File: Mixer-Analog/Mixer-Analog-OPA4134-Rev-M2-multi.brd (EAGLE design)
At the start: 123 x 51 mm, 119 parts, among them IC1 BQ297X, IC2 MCP73831, IC3 QS6K1, IC4 OPA4134D, IC5 SC4503, IC6 TPS7A49, J10 PHONES-OUT, J11 12V, J7 Battery, J9 LINE-OUT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

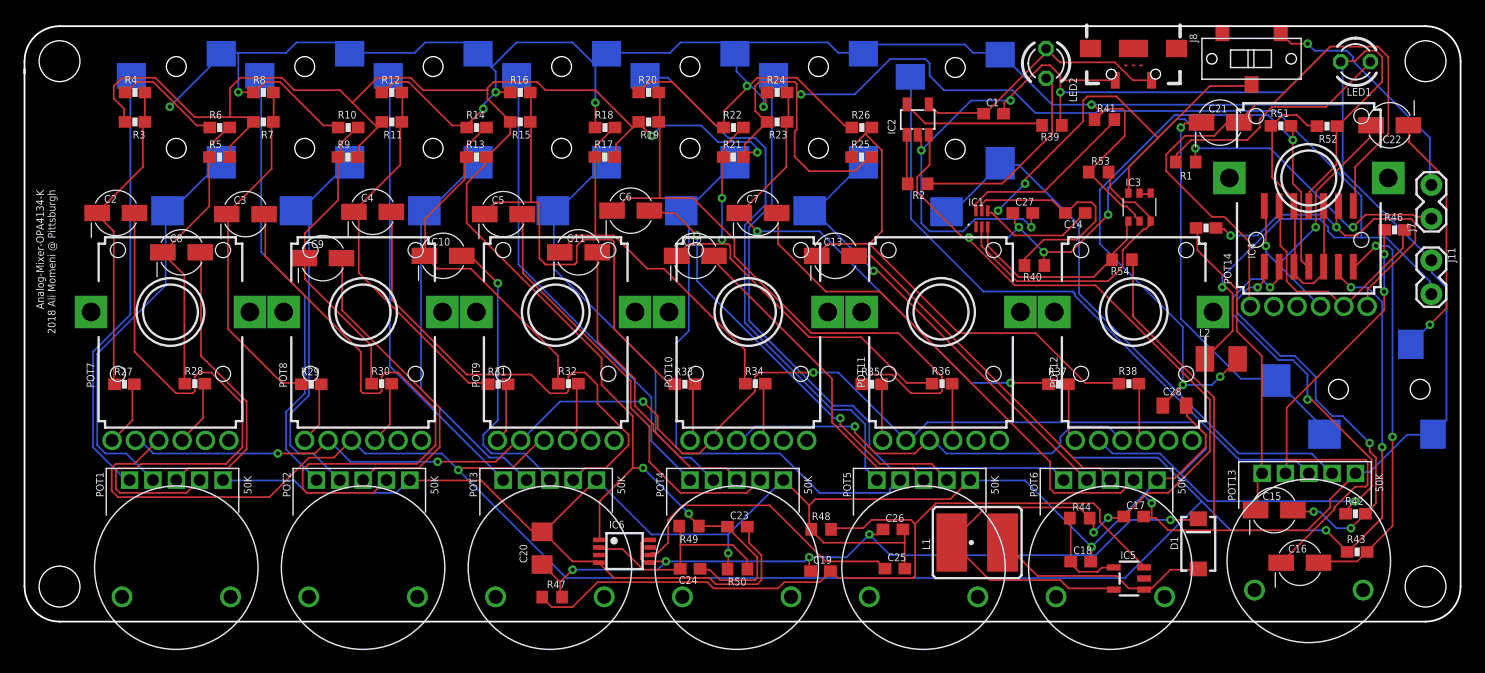
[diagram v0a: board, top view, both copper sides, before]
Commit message: Multiple updates
Rev-M updated for change of capacitors from tantalum to electrolytic.
Rev-M2 created based on the new schematic provided.
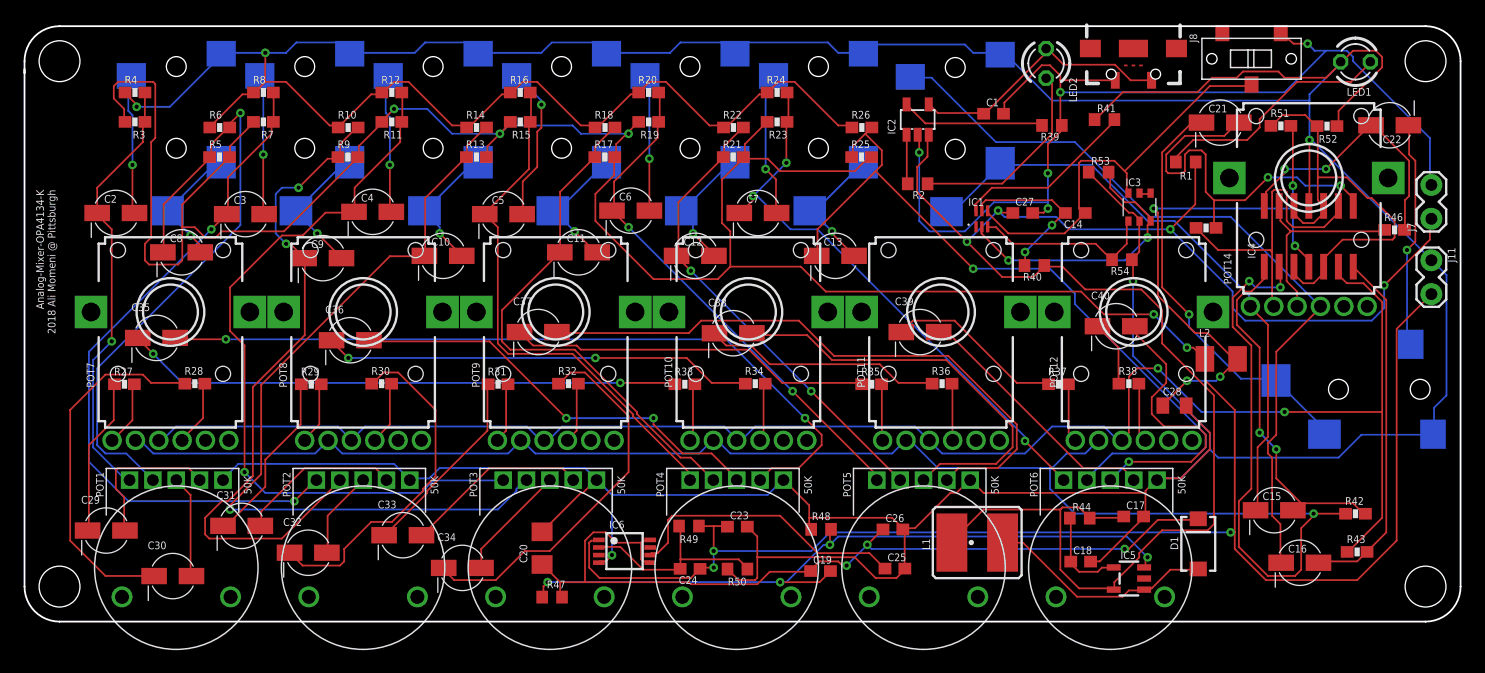
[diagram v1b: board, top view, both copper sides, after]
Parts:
- removed POT13: 50K, CMU-ArtFab:POT-DUAL-ALPS-RK10J12E0A0A
- added C29, C30, C31, C32, C33, C34, C35, C36, C37, C38, C39, C40: 10uF, CMU-ArtFab:PANASONIC_B
- R45, R46: value 47K -> 100K
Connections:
- removed net N$16: J9.2, J9.4, POT13.P$2
- removed net N$18: J9.3, POT13.P$3
- removed net N$76: J5.3, POT5.P$5
- removed net N$80: J5.2, J5.4, POT5.P$4
- removed net N$92: J6.3, POT6.P$5
- removed net N$96: J6.2, J6.4, POT6.P$4
- new net N$20: C30.-, R28.1
- new net N$35: C29.-, R27.1
- new net N$36: C32.-, R30.1
- new net N$37: C32.+, POT2.P$3
- new net N$38: C33.+, POT3.P$2
- new net N$39: C33.-, R31.1
- new net N$40: C34.-, R32.1
- new net N$49: C36.+, POT4.P$3
- new net N$50: C35.-, R33.1
- new net N$51: C36.-, R34.1
- new net N$52: C37.+, POT5.P$2
- new net N$53: C37.-, R35.1
- new net N$54: C38.+, POT5.P$3
- new net N$56: C38.-, R36.1
- new net N$57: C39.+, POT6.P$2
- new net N$67: C40.+, POT6.P$3
- net GND: no longer POT13.P$1
- net N$1: now also J1.2, J1.4; no longer POT1.P$3
- net N$13: now also POT1.P$5; no longer R27.1
- net N$15: now also POT14.2.1, R46.1; no longer POT14.2.3, R46.2
- net N$22: now also POT2.P$4; no longer R30.1
- net N$24: now also R45.2; no longer POT14.1.2
- net N$25: now also R46.2; no longer POT14.2.2
- net N$26: now also C31.+, POT2.P$2; no longer J2.3, POT2.P$5
- net N$28: now also J2.2, J2.4; no longer POT2.P$3
- net N$29: now also J2.3; no longer POT2.P$2
- net N$3: now also POT1.P$4; no longer R28.1
- net N$30: now also C31.-, R29.1; no longer J2.2, J2.4, POT2.P$4
- net N$31: now also POT2.P$5; no longer R29.1
- net N$41: now also POT3.P$4; no longer R32.1
- net N$42: now also C34.+, POT3.P$3; no longer J3.3, POT3.P$5
- net N$44: now also J3.2, J3.4; no longer POT3.P$3
- net N$45: now also J3.3; no longer POT3.P$2
- net N$46: now also C35.+, POT4.P$2; no longer J3.2, J3.4, POT3.P$4
- net N$47: now also POT3.P$5; no longer R31.1
- net N$5: now also C29.+, POT1.P$2; no longer J1.3, POT1.P$5
- net N$58: now also POT4.P$4; no longer R34.1
- net N$59: now also C39.-, R37.1; no longer J4.3, POT4.P$5
- net N$61: now also J9.2, J9.4, POT14.1.2; no longer POT13.P$5, R45.1
- net N$62: now also J4.2, J4.4; no longer POT4.P$3
- net N$63: now also J4.3; no longer POT4.P$2
- net N$64: now also C40.-, R38.1; no longer J4.2, J4.4, POT4.P$4
- net N$65: now also POT4.P$5; no longer R33.1
- net N$75: now also POT5.P$4; no longer R36.1
- net N$78: now also J5.2, J5.4; no longer POT5.P$3
- net N$79: now also J5.3; no longer POT5.P$2
- net N$8: now also J1.3; no longer POT1.P$2
- net N$81: now also POT5.P$5; no longer R35.1
- net N$9: now also C30.+, POT1.P$3; no longer J1.2, J1.4, POT1.P$4
- net N$91: now also POT6.P$4; no longer R38.1
- net N$94: now also J6.2, J6.4; no longer POT6.P$3
- net N$95: now also J6.3; no longer POT6.P$2
- net N$97: now also POT6.P$5; no longer R37.1
- net OUT-L1: now also POT14.1.1, R45.1; no longer POT14.1.3, R45.2
- net OUT-R1: now also J9.3, POT14.2.2; no longer POT13.P$4, R46.1
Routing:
- net OUT-R: track 212.5 -> 145.8 mm, vias 5 -> 2
- net N$92: track 55.7 -> 0.00 mm
- net N$18: track 55.4 -> 0.00 mm
- net N$52: track 0.00 -> 52.8 mm
- net N$16: track 49.2 -> 0.00 mm
- net N$80: track 49.2 -> 0.00 mm
- net N$76: track 47.7 -> 0.00 mm
- net N$50: track 0.00 -> 47.7 mm, vias 0 -> 2
- net N$29: track 52.5 -> 12.0 mm, vias 0 -> 1
- net N$96: track 39.6 -> 0.00 mm, vias 1 -> 0
- net N$41: track 30.6 -> 70.1 mm, vias 0 -> 1
- net N$8: track 49.9 -> 12.1 mm, vias 0 -> 1
- net N$51: track 0.00 -> 37.0 mm, vias 0 -> 2
- net N$49: track 0.00 -> 36.9 mm, vias 0 -> 2
- net N$54: track 0.00 -> 36.2 mm
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
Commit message: pot reference changed in both boards
The pot side hole size update was not reflected in the boards. now they are referenced to the latest version of the device.
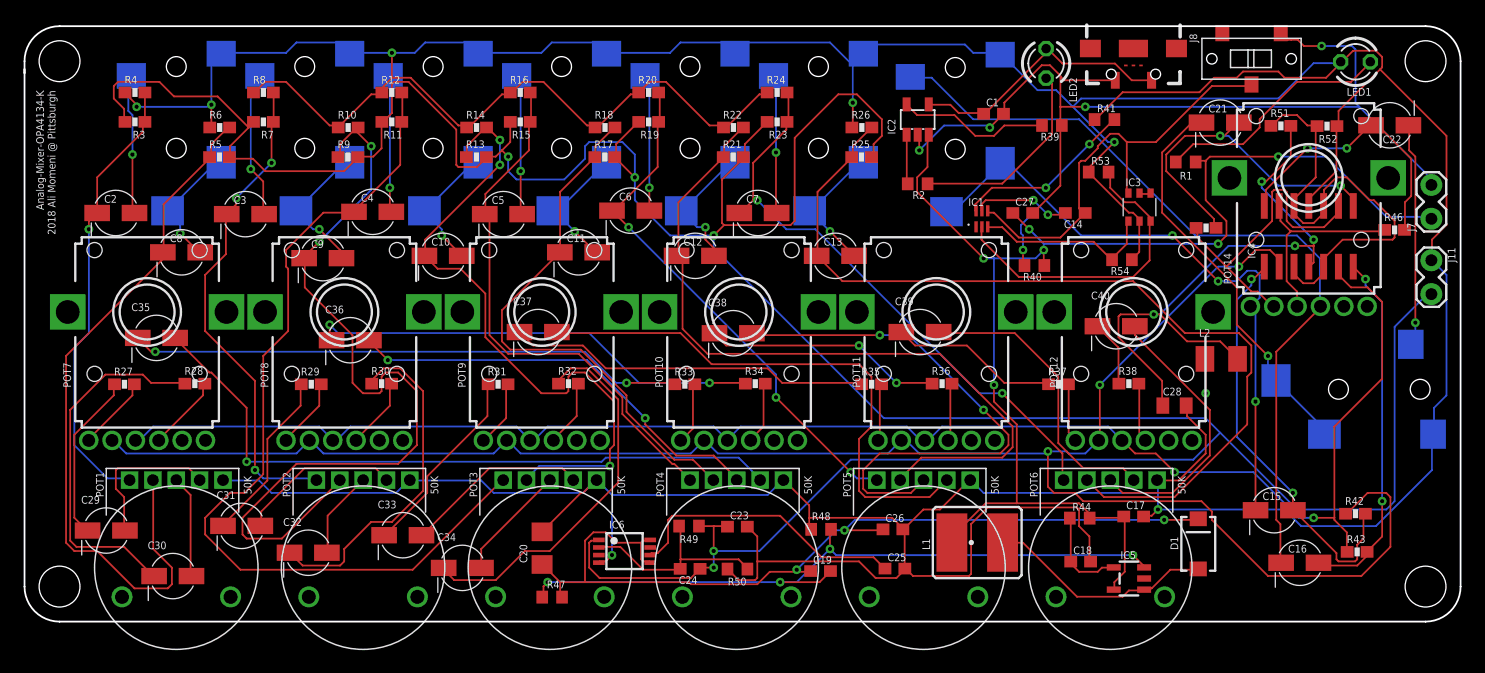
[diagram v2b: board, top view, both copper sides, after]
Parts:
- moved POT7 2.00 mm to (10.5, 26.5)
- moved POT8 1.60 mm to (27.4, 26.5)
- moved POT9 1.20 mm to (44.3, 26.5)
- moved POT10 0.80 mm to (61.2, 26.5)
- moved POT11 0.40 mm to (78.1, 26.5)
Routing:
- net VBAT: track 149.2 -> 115.7 mm, vias 4 -> 6
- net N$75: track 40.6 -> 64.3 mm, vias 2 -> 0
- net N$31: track 59.8 -> 42.2 mm, vias 2 -> 3
- net N$22: track 58.2 -> 72.3 mm
- net N$41: track 70.1 -> 56.6 mm, vias 1 -> 3
- net +12V: track 306.2 -> 293.1 mm, vias 8 -> 6
- net GND: track 465.1 -> 478.0 mm, vias 5 -> 7
- net N$47: track 64.9 -> 77.2 mm, vias 1 -> 0
- net N$54: track 36.2 -> 47.2 mm, vias 0 -> 2
- net N$91: track 67.2 -> 77.2 mm, vias 1 -> 0
- net N$46: track 66.2 -> 58.2 mm, vias 2 -> 1
- net USBGND: track 90.5 -> 82.8 mm, vias 5 -> 4
- net N$3: track 54.5 -> 61.9 mm, vias 1 -> 0
- net OUT-R: track 145.8 -> 139.5 mm
- net N$52: track 52.8 -> 47.1 mm
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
